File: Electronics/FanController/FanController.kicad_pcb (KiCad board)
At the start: 2 copper layers, 43 parts, among them J1 POWER IN, J2 CONTROLLER IN/OUT, J3 PROGRAMMER, J4 SUPPLY SELECTOR, J5 FAN I/O, Q1 PMOS, Q2 PMOS, SW1 RST_BUTTON, U1 DRV8871DDA, U3 INA240A3D, U4 STM32L051K8Tx, Y2 CM8V-T1A-32.768KHZ

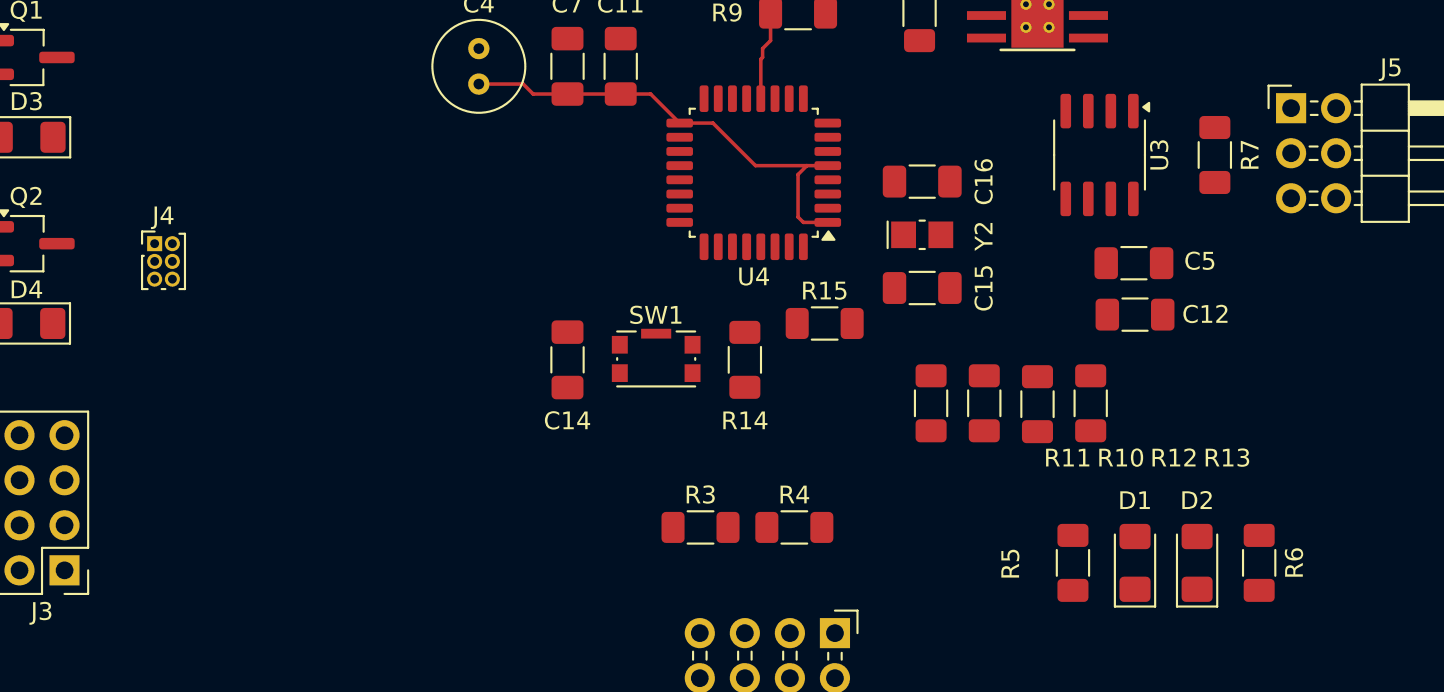
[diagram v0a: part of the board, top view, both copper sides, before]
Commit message: Changed schematic
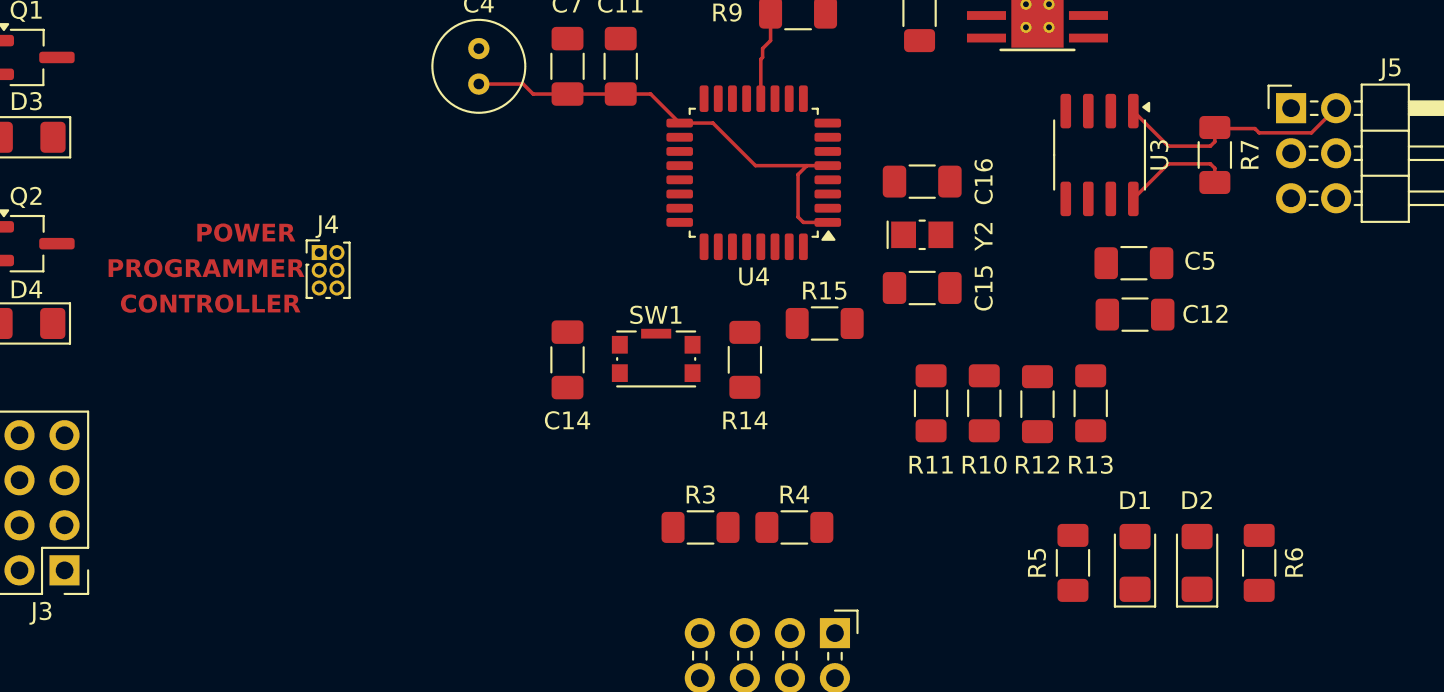
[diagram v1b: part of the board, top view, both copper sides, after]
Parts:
- moved J4 9.29 mm to (55.0, 40.5)
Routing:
- net /Power_and_IO/OUT1: track 0.00 -> 13.9 mm
- net /Power_and_IO/OUT1+: track 0.00 -> 6.32 mm
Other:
- board text added: "CONTROLLER"
- board text added: "POWER"
- board text added: "PROGRAMMER"
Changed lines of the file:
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@@
 		)
 		(property "Value" "100 nF"
-			(at 0 1.85 360)
+			(at 0 1.85 0)
 			(layer "F.Fab")
 			(hide yes)
@@
 		)
 		(fp_text user "${REFERENCE}"
-			(at 0 0 360)
+			(at 0 0 0)
 			(layer "F.Fab")
 			(effects
@@
 		)
 		(property "Value" "100 nF"
-			(at 0 1.85 270)
+			(at 0 1.85 -90)
 			(layer "F.Fab")
 			(hide yes)
@@
 		)
 		(fp_text user "${REFERENCE}"
-			(at 0 0 270)
+			(at 0 0 -90)
 			(layer "F.Fab")
 			(effects
@@
 		)
 		(property "Value" "CM8V-T1A-32.768KHZ"
-			(at 0 1.8 360)
+			(at 0 1.8 0)
 			(layer "F.Fab")
 			(hide yes)
@@
 		)
 		(fp_text user "${REFERENCE}"
-			(at 0 0 360)
+			(at 0 0 0)
 			(layer "F.Fab")
 			(effects
@@
 		)
 		(property "Value" "100 nF"
-			(at 0 1.85 270)
+			(at 0 1.85 -90)
 			(layer "F.Fab")
 			(hide yes)
@@
 		)
 		(fp_text user "${REFERENCE}"
-			(at 0 0 270)
+			(at 0 0 -90)
 			(layer "F.Fab")
 			(effects
@@
 	)
 	(footprint "Resistor_SMD:R_1206_3216Metric_Pad1.30x1.75mm_HandSolder"
+		(locked yes)
 		(layer "F.Cu")
 		(at 105.5 35 90)
@@
 		(tags "resistor handsolder")
 		(property "Reference" "R7"
-			(at 0 2 270)
+			(at 0 2 -90)
 			(layer "F.SilkS")
 			(effects
@@
 		)
 		(property "Value" "0R006"
-			(at -0.5 19 270)
+			(at -0.5 19 -90)
 			(layer "F.Fab")
 			(effects
@@
 		)
 		(fp_text user "${REFERENCE}"
-			(at 0 0 270)
+			(at 0 0 -90)
 			(layer "F.Fab")
 			(effects
@@
 		(tags "resistor handsolder")
 		(property "Reference" "R6"
-			(at 0 2 270)
+			(at 0 2 -90)
 			(layer "F.SilkS")
 			(effects
@@
 		)
 		(property "Value" "220 R"
-			(at 0 3.5 270)
+			(at 0 3.5 -90)
 			(layer "F.Fab")
+			(hide yes)
 			(effects
 				(font
@@
 		)
 		(fp_text user "${REFERENCE}"
-			(at 0 0 270)
+			(at 0 0 -90)
 			(layer "F.Fab")
 			(effects
@@
 		)
 		(fp_text user "${REFERENCE}"
-			(at 0 0 270)
+			(at 0 0 -90)
 			(layer "F.Fab")
 			(effects
@@
 		)
 		(fp_text user "${REFERENCE}"
-			(at 5.31 1.27 270)
+			(at 5.31 1.27 -90)
 			(layer "F.Fab")
 			(effects
@@
 		(tags "capacitor handsolder")
 		(property "Reference" "C13"
-			(at -3.5 0 360)
+			(at -3.5 0 0)
 			(layer "F.SilkS")
 			(effects
@@
 		)
 		(property "Value" "100 nF"
-			(at 0 -3.5 360)
+			(at 0 -3.5 0)
 			(layer "F.Fab")
 			(hide yes)
@@
 		)
 		(fp_text user "${REFERENCE}"
-			(at 0 0 360)
+			(at 0 0 0)
 			(layer "F.Fab")
 			(effects
@@
 		(tags "resistor handsolder")
 		(property "Reference" "R13"
-			(at 3.1 -7.7 180)
+			(at 3.5 0 180)
 			(layer "F.SilkS")
 			(effects
@@
 		)
 		(property "Value" "10 uF"
-			(at 1 3.75 270)
+			(at 1 3.75 -90)
 			(layer "F.Fab")
 			(hide yes)
@@
 		)
 		(fp_text user "${REFERENCE}"
-			(at 1 0 270)
+			(at 1 0 -90)
 			(layer "F.Fab")
 			(effects
@@
 		(tags "resistor handsolder")
 		(property "Reference" "R11"
-			(at -3.1 7.7 0)
+			(at -3.5 0 0)
 			(layer "F.SilkS")
 			(effects
@@
 		)
 		(property "Value" "7.5k"
-			(at 0 -3.5 270)
+			(at 0 -3.5 -90)
 			(layer "F.Fab")
 			(hide yes)
@@
 		)
 		(fp_text user "${REFERENCE}"
-			(at 0 0 270)
+			(at 0 0 -90)
 			(layer "F.Fab")
 			(effects
@@
 	(footprint "Connector_PinHeader_1.00mm:PinHeader_2x03_P1.00mm_Vertical"
 		(layer "F.Cu")
-		(at 45.72 40)
+		(at 55 40.5)
 		(descr "Through hole straight pin header, 2x03, 1.00mm pitch, double rows")
 		(tags "Through hole pin header THT 2x03 1.00mm double row")
@@
 		)
 		(property "Value" "SUPPLY SELECTOR"
-			(at 0.5 3.56 0)
+			(at 0.5 4.5 0)
 			(layer "F.Fab")
+			(hide yes)
 			(effects
 				(font
@@
 		(tags "resistor handsolder")
 		(property "Reference" "R5"
-			(at -0.05 -3.5 270)
+			(at 0 -2 -90)
 			(layer "F.SilkS")
 			(effects
@@
 		)
 		(property "Value" "220 R"
-			(at -0.05 -2 270)
+			(at -0.05 -2 -90)
 			(layer "F.Fab")
+			(hide yes)
 			(effects
 				(font
@@
 		)
 		(fp_text user "${REFERENCE}"
-			(at 0 0 270)
+			(at 0 0 -90)
 			(layer "F.Fab")
 			(effects
@@
 	)
 	(footprint "Package_SO:SOIC-8_3.9x4.9mm_P1.27mm"
+		(locked yes)
 		(layer "F.Cu")
 		(at 99 35 -90)
@@
 		(tags "resistor handsolder")
 		(property "Reference" "R10"
-			(at 3.1 -7.7 180)
+			(at 3.5 0 180)
 			(layer "F.SilkS")
 			(effects
@@
 		(tags "capacitor handsolder")
 		(property "Reference" "C15"
-			(at -3.5 0 270)
+			(at -3.5 0 -90)
 			(layer "F.SilkS")
 			(effects
@@
 		)
 		(property "Value" "30k"
-			(at 0 1.82 270)
+			(at 0 1.82 -90)
 			(layer "F.Fab")
 			(hide yes)
@@
 		)
 		(fp_text user "${REFERENCE}"
-			(at 0 0 270)
+			(at 0 0 -90)
 			(layer "F.Fab")
 			(effects
@@
 		(tags "resistor handsolder")
 		(property "Reference" "R12"
-			(at -3.05 7.7 0)
+			(at -3.45 0 0)
 			(layer "F.SilkS")
 			(effects
@@
 		)
 		(property "Value" "22k"
-			(at 0 1.82 270)
+			(at 0 1.82 -90)
 			(layer "F.Fab")
 			(hide yes)
@@
 		)
 		(fp_text user "${REFERENCE}"
-			(at 0 0 270)
+			(at 0 0 -90)
 			(layer "F.Fab")
 			(effects
@@
 		)
 		(fp_text user "${REFERENCE}"
-			(at 1.27 3.81 270)
+			(at 1.27 3.81 -90)
 			(layer "F.Fab")
 			(effects
@@
 		)
 		(fp_text user "${REFERENCE}"
-			(at 0 0 270)
+			(at 0 0 -90)
 			(layer "F.Fab")
 			(effects
@@
 		)
 	)
+	(gr_text "POWER"
+		(at 48 40 0)
+		(layer "F.Cu")
+		(effects
+			(font
+				(size 1 1)
+				(thickness 0.2)
+				(bold yes)
+			)
+			(justify left bottom)
+		)
+	)
+	(gr_text "PROGRAMMER"
+		(at 43 42 0)
+		(layer "F.Cu")
+		(effects
+			(font
+				(size 1 1)
+				(thickness 0.2)
+				(bold yes)
+			)
+			(justify left bottom)
+		)
+	)
+	(gr_text "CONTROLLER"
+		(at 43.75 44 0)
+		(layer "F.Cu")
+		(effects
+			(font
+				(size 1 1)
+				(thickness 0.2)
+				(bold yes)
+			)
+			(justify left bottom)
+		)
+	)
 	(segment
 		(start 73.6875 31.5625)
@@
 		(net 4)
 	)
+	(segment
+		(start 105.56 33.51)
+		(end 107.76 33.51)
+		(width 0.2)
+		(layer "F.Cu")
+		(net 30)
+	)
+	(segment
+		(start 105.5 34.25)
+		(end 105.5 33.45)
+		(width 0.2)
+		(layer "F.Cu")
+		(net 30)
+	)
+	(segment
+		(start 100.905 32.525)
+		(end 102.88 34.5)
+		(width 0.2)
+		(layer "F.Cu")
+		(net 30)
+	)
+	(segment
+		(start 108 33.75)
+		(end 110.95 33.75)
+		(width 0.2)
+		(layer "F.Cu")
+		(net 30)
+	)
+	(segment
+		(start 105.25 34.5)
+		(end 105.5 34.25)
+		(width 0.2)
+		(layer "F.Cu")
+		(net 30)
+	)
+	(segment
+		(start 110.95 33.75)
+		(end 112.34 32.36)
+		(width 0.2)
+		(layer "F.Cu")
+		(net 30)
+	)
+	(segment
+		(start 105.5 33.45)
+		(end 105.56 33.51)
+		(width 0.2)
+		(layer "F.Cu")
+		(net 30)
+	)
+	(segment
+		(start 102.88 34.5)
+		(end 105.25 34.5)
+		(width 0.2)
+		(layer "F.Cu")
+		(net 30)
+	)
+	(segment
+		(start 107.76 33.51)
+		(end 108 33.75)
+		(width 0.2)
+		(layer "F.Cu")
+		(net 30)
+	)
+	(segment
+		(start 102.88 35.5)
+		(end 105.25 35.5)
+		(width 0.2)
+		(layer "F.Cu")
+		(net 35)
+	)
+	(segment
+		(start 105.25 35.5)
+		(end 105.5 35.75)
+		(width 0.2)
+		(layer "F.Cu")
+		(net 35)
+	)
+	(segment
+		(start 105.5 35.75)
+		(end 105.5 36.55)
+		(width 0.2)
+		(layer "F.Cu")
+		(net 35)
+	)
+	(segment
+		(start 100.905 37.475)
+		(end 102.88 35.5)
+		(width 0.2)
+		(layer "F.Cu")
+		(net 35)
+	)
 )

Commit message: Routed PCB-layout
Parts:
- removed D3, D4: D, Diode_SMD:D_1206_3216Metric_Pad1.42x1.75mm_HandSolder
- removed Q1, Q2: PMOS, Package_TO_SOT_SMD:TSOT-23_HandSoldering
- removed R1, R2: 1M, Resistor_SMD:R_1206_3216Metric_Pad1.30x1.75mm_HandSolder
- C11, C12, C14, C15, C16, C2, C3, C5, C7, R10, R11, R12, R13, R14, R15, R3, R4, R5, R6, R8: moved to B.Cu
- J4: footprint Connector_PinHeader_1.00mm:PinHeader_2x03_P1.00mm_Vertical -> Connector_PinHeader_2.54mm:PinHeader_2x03_P2.54mm_Vertical
- moved R13 68.3 mm to (37.0, 19.2), turned to 90 degrees
- moved R12 63.1 mm to (40.0, 19.0), turned to -90 degrees
- moved C3 59.5 mm to (58.5, 35.5)
- moved R10 57.9 mm to (43.0, 18.9)
- moved R4 57.0 mm to (31.2, 29.8), turned to 180 degrees
- moved C5 54.8 mm to (50.4, 20.0), turned to 180 degrees
- moved J5 52.7 mm to (59.1, 18.0)
- moved R11 52.7 mm to (46.0, 19.3)
- moved R7 52.3 mm to (55.2, 20.6)
- moved C1 51.4 mm to (61.5, 34.5)
- moved R3 51.1 mm to (31.2, 32.2), turned to 180 degrees
- moved U3 50.3 mm to (50.8, 20.6)
- moved C12 49.3 mm to (55.2, 25.5)
- moved D1 46.3 mm to (57.5, 42.0)
- moved D2 46.3 mm to (61.0, 42.0)
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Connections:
- J1 pad 1: +12V -> +3.3V
- J1 pad 3: +3.3V -> +12P
- J2 pad 1: VD -> GND
- J2 pad 7: GND -> VD
- J3 pad 2: /mcu/NRST -> VDD
- J3 pad 8: VDD -> /mcu/NRST
- J4 pad 2: +3.3VA -> +3.3VP
- J4 pad 4: +3.3VA -> +3.3VP
- J4 pad 6: +3.3VA -> +3.3VP
- J5 pad 2: /Power_and_IO/OUT1 -> /Power_and_IO/PULSE_01_12V
- J5 pad 3: GND -> /Power_and_IO/OUT1
- J5 pad 4: /Power_and_IO/OUT2 -> /Power_and_IO/PULSE_02_12V
- J5 pad 5: /Power_and_IO/PULSE_01_12V -> GND
- J5 pad 6: /Power_and_IO/PULSE_02_12V -> /Power_and_IO/OUT2
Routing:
- net +12P: track 0.00 -> 90.6 mm, vias 0 -> 12
- net /mcu/NRST: track 0.00 -> 53.1 mm, vias 0 -> 5
- net +3.3VP: track 26.5 -> 76.9 mm, vias 0 -> 6
- net GND: track 0.00 -> 34.6 mm, vias 0 -> 7
- net /Power_and_IO/PULSE_01_12V: track 0.00 -> 28.4 mm, vias 0 -> 2
- net /Power_and_IO/LED_RED: track 0.00 -> 27.1 mm
- net /Power_and_IO/PULSE_02_12V: track 0.00 -> 24.3 mm, vias 0 -> 2
- net /Power_and_IO/LED_GREEN: track 0.00 -> 24.2 mm
- net /mcu/SWCLK: track 0.00 -> 22.9 mm, vias 0 -> 1
- net /Power_and_IO/SDA: track 0.00 -> 21.9 mm, vias 0 -> 2
- net /Power_and_IO/OUT2: track 0.00 -> 21.9 mm, vias 0 -> 4
- net /mcu/SWDIO: track 0.00 -> 21.3 mm, vias 0 -> 1
- net /mcu/UART_TX: track 0.00 -> 19.9 mm, vias 0 -> 1
- net +3.3V: track 0.00 -> 18.6 mm, vias 0 -> 2
- net /Power_and_IO/SCL: track 0.00 -> 18.1 mm, vias 0 -> 1
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- added copper zone on B.Cu, net GND
- added copper zone on F.Cu, net GND
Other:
- board outline added: 50 x 30 mm
- board text added: "CO"
- board text added: "PO"
- board text added: "PR"
- board text removed: "CONTROLLER"
- board text removed: "POWER"
- board text removed: "PROGRAMMER"

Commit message: Finished routing
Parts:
- moved C16 0.70 mm to (49.1, 27.0)
- moved Y2 0.55 mm to (49.2, 28.8)
- moved C15 0.14 mm to (49.1, 30.6)
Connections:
- Y2 pad 1: (no net) -> /mcu/OSC_OUT
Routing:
- net /mcu/OSC_OUT: track 4.84 -> 6.06 mm

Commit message: Finialized Circuitboard
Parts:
- moved C14 1.75 mm to (51.0, 36.8)
- moved R14 1.75 mm to (48.5, 36.8)
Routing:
- net GND: track 34.6 -> 28.9 mm, vias 7 -> 9
- net /mcu/NRST: track 53.1 -> 51.3 mm
- net +3.3VP: track 76.8 -> 76.0 mm
